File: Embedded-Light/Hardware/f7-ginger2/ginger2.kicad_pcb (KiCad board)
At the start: 2 copper layers, 84 x 57 mm, 75 parts, among them P1 USB_OTG, P2 USB_A, P3 SWD, P4 microSD, P5 BATR, SW1 RST, SW2 B4, SW3 B3, SW4 B2, SW5 B1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

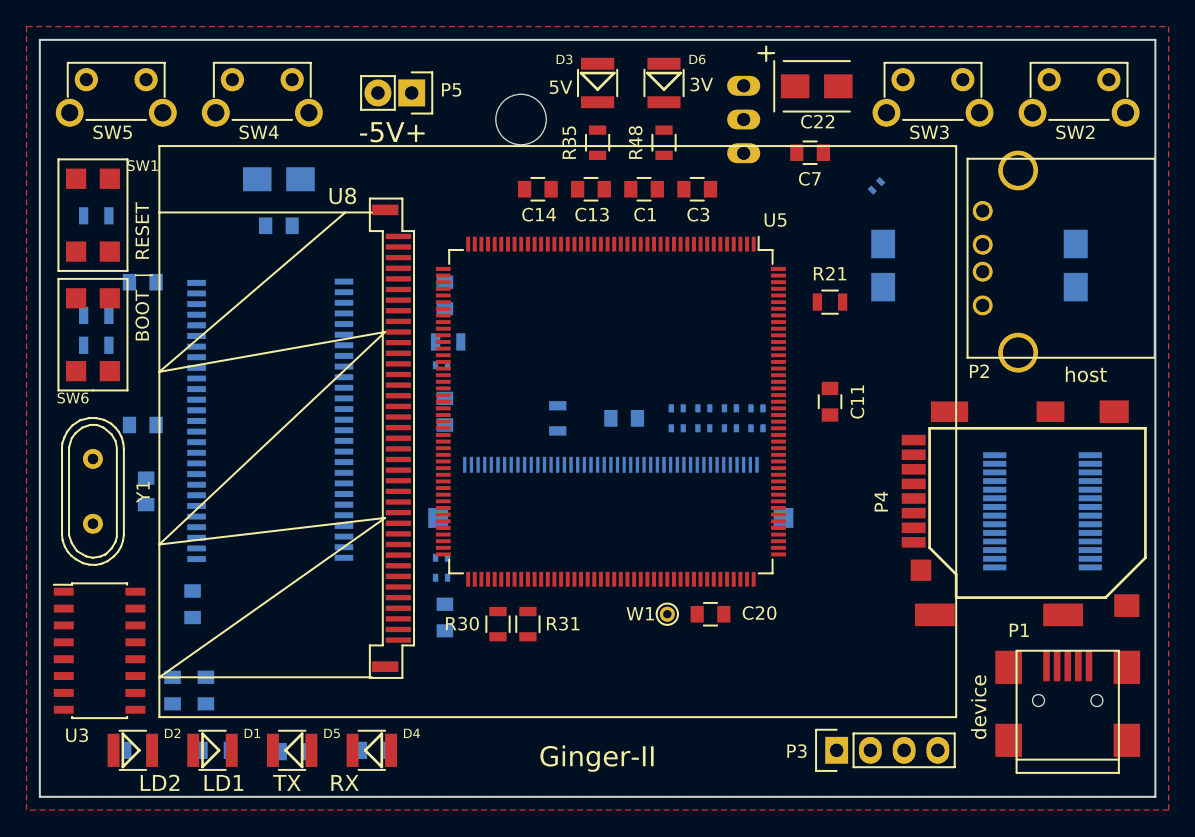
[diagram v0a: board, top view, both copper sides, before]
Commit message: Ginger2: new board schematics and placement, ready to route.
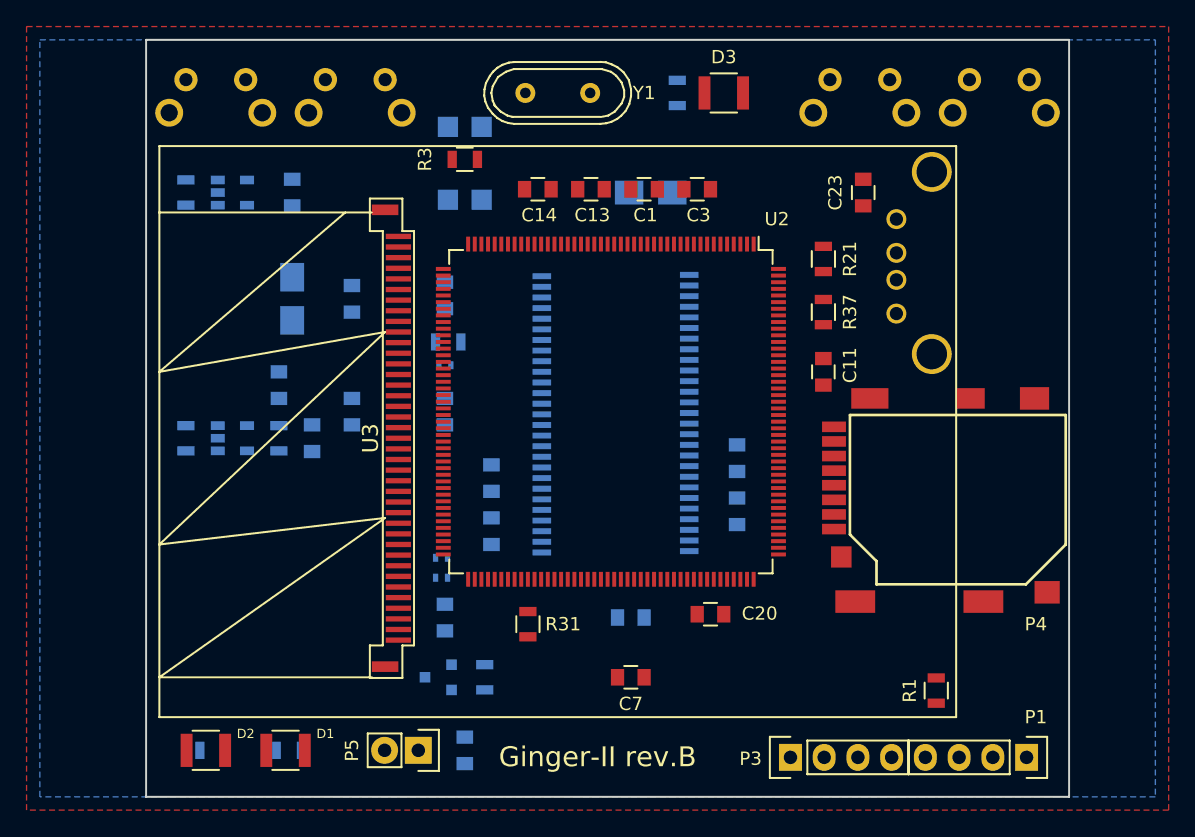
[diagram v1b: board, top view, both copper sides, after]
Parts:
- removed D4: RX, Resistors_SMD:R_1210
- removed D5: TX, Resistors_SMD:R_1210
- removed D6: 3V, Resistors_SMD:R_1210
- removed DD7: MT48LC16M16A2, tsop-54:TSOP-54
- removed R30, R53: 1k, Resistors_SMD:R_0805
- removed R33, R35: 510, Resistors_SMD:R_0805
- removed R38, R39, R48: 330, Resistors_SMD:R_0805
- removed R40, R43, R44, R46: 0, Resistors_SMD:R_0402
- removed R41, R42, R45, R47: DNP, Resistors_SMD:R_0402
- removed SW6: BOOT, button_bourns:but_7914G
- removed U6: FT232RL, Housings_SSOP:SSOP-28_5.3x10.2mm_Pitch0.65mm
- removed U7: LM2937-3.3, TO_SOT_Packages_THT:TO-220_Neutral123_Horizontal
- removed U8: WF24HTLAJDNN0, TFT-WF24HTLAJDNN:FPC_39
- removed U9: DT022CTFT, XF2M45151A:XF2M45151A
- removed W1: MCO, Connect:PINTST
- added C23: 100n, Capacitors_SMD:C_0805, F.Cu at (163.0, 70.5)
- added C24: 10u, Capacitors_SMD:C_0805, B.Cu at (121.5, 89.0)
- added L1: 2.2uH, Resistors_SMD:R_0805, B.Cu at (119.0, 89.0)
- added Q1: FDN337N, TO_SOT_Packages_SMD:SOT-23, B.Cu at (131.0, 107.0)
- added R2: 10k, Resistors_SMD:R_0805, B.Cu at (134.5, 107.0)
- added R4: 10k, Resistors_SMD:R_0805, B.Cu at (112.0, 70.5)
- added R5: 1k, Resistors_SMD:R_0805, B.Cu at (112.0, 89.0)
- added R6: 510, Resistors_SMD:R_0805, B.Cu at (149.0, 63.0)
- added U1: MT48LC16M16A2, tsop-54:TSOP-54, B.Cu at (144.5, 87.5)
- added U2: STM32F767IIT6, Housings_QFP:LQFP-176_24x24mm_Pitch0.5mm, F.Cu at (144.0, 87.0)
- added U4: LM3671MF-FIX, TO_SOT_Packages_SMD:SOT-23-5, B.Cu at (115.5, 89.0)
- C21: value 47u -> 4.7u; footprint Capacitors_Tantalum_SMD:TantalC_SizeB_EIA-3528_Wave -> Capacitors_SMD:C_0805
- C22: value 47u -> 10n; footprint Capacitors_Tantalum_SMD:TantalC_SizeB_EIA-3528_Wave -> Capacitors_SMD:C_0805; moved to B.Cu
- D3: value 5V -> PWR
- P1: value USB_OTG -> UART; footprint Connect:USB_Mini-B -> Pin_Headers:Pin_Header_Straight_1x04
- P2: value USB_A -> USB_HOST; moved to B.Cu
- P5: value BATR -> BAT
- R1: value 0 -> 1k; footprint Resistors_SMD:R_0402 -> Resistors_SMD:R_0805; moved to F.Cu
- R3, R37: moved to F.Cu
- SW1, SW2, SW3, SW4, SW5: moved to B.Cu
- U3: value ULN2003A -> WF24HTLAJDNN0; footprint Housings_SOIC:SOIC-16_3.9x9.9mm_Pitch1.27mm -> TFT-WF24HTLAJDNN:FPC_39
- U5: value STM32F767IIT6 -> LP2985LV; footprint Housings_QFP:LQFP-176_24x24mm_Pitch0.5mm -> TO_SOT_Packages_SMD:SOT-23-5; moved to B.Cu
- moved C21 58.7 mm to (133.0, 112.5)
- moved R37 54.8 mm to (160.0, 79.5), turned to 270 degrees
- moved P5 49.5 mm to (129.5, 112.5)
- moved Y1 46.1 mm to (140.0, 63.0), turned to 180 degrees
- moved C12 44.6 mm to (153.5, 90.5)
- moved C7 41.7 mm to (145.5, 107.0)
- moved C2 41.6 mm to (153.5, 94.5)
- moved C22 40.3 mm to (120.0, 70.5), turned to 270 degrees
- moved R1 38.3 mm to (168.5, 108.0), turned to 270 degrees
- moved U5 32.9 mm to (115.5, 70.5), turned to 0 degrees
- moved C8 32.3 mm to (135.0, 96.0), turned to 90 degrees
- moved C6 31.5 mm to (124.5, 78.5)
- moved SW1 28.2 mm to (133.0, 68.5)
- moved R3 28.1 mm to (133.0, 68.0)
- moved U3 27.6 mm to (128.0, 89.0), turned to 270 degrees
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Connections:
- C22 pad 1: +3V3 -> Net-(C22-Pad1)
- D3 pad 2: +5V -> +3V3
- P1 pad 1: +5V -> Net-(P1-Pad1)
- P1 pad 4: (no net) -> GND
- P5 pad 1: +5V -> Net-(C21-Pad1)
- R1 pad 1: Net-(C21-Pad1) -> /cpu_boot
- R1 pad 2: +5V -> Net-(P1-Pad3)
- U3 pad 1: /pwm_ch1 -> GND
- U3 pad 10: (no net) -> /tft_cs
- U3 pad 11: (no net) -> /tft_rs
- U3 pad 12: (no net) -> /tft_wr
- U3 pad 13: /LCD2_LK3 -> Net-(R49-Pad1)
- U3 pad 14: /LCD2_LK1 -> /sdr_d0
- U3 pad 15: /LCD1_LK3 -> /sdr_d1
- U3 pad 16: /LCD1_LK1 -> /sdr_d2
- U3 pad 2: /pwm_ch1 -> (no net)
- U3 pad 3: /pwm_ch2 -> (no net)
- U3 pad 4: /pwm_ch2 -> (no net)
- U3 pad 5: GND -> (no net)
- U3 pad 6: GND -> (no net)
- U3 pad 7: GND -> +3V3
- U3 pad 8: GND -> +3V3
- U3 pad 9: +3V3 -> /tft_fsync
- U5 pad 1: Net-(SW5-Pad2) -> Net-(C21-Pad1)
- U5 pad 2: Net-(SW4-Pad2) -> GND
- U5 pad 3: Net-(SW3-Pad2) -> /usb_pon
- U5 pad 4: Net-(SW2-Pad2) -> Net-(C22-Pad1)
- U5 pad 5: (no net) -> +5V
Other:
- board size 84 x 57 mm -> 69.5 x 57 mm
- board text added: "Ginger-II rev.B"
- board text removed: "-5V+"
- board text removed: "3V"
- board text removed: "5V"
- board text removed: "BOOT | RESET"
- board text removed: "LD2 LD1 TX RX"
- board text removed: "device"
- board text removed: "host"

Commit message: Ginger2: rev.B routed.
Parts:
- moved C15 12.7 mm to (119.0, 98.5)
- moved C6 10.0 mm to (114.5, 79.0)
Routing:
- net GND: track 0.00 -> 519.5 mm, vias 0 -> 5
- net +3V3: track 0.00 -> 411.9 mm, vias 0 -> 4
- net /tft_rs: track 0.00 -> 113.9 mm, vias 0 -> 2
- net /cpu_rst: track 0.00 -> 94.4 mm, vias 0 -> 1
- net /tft_cs: track 0.00 -> 88.6 mm
- net /sdr_d13: track 0.00 -> 84.9 mm, vias 0 -> 2
- net /sdr_d14: track 0.00 -> 82.4 mm, vias 0 -> 2
- net /sdr_d1: track 0.00 -> 72.7 mm, vias 0 -> 2
- net +5V: track 0.00 -> 63.5 mm
- net Net-(SW5-Pad2): track 0.00 -> 57.0 mm
- net Net-(C21-Pad1): track 0.00 -> 56.1 mm
- net Net-(SW4-Pad2): track 0.00 -> 45.9 mm
- net Net-(P1-Pad2): track 0.00 -> 45.3 mm
- net /cpu_boot: track 0.00 -> 40.7 mm
- net Net-(Q1-Pad1): track 0.00 -> 40.6 mm, vias 0 -> 1
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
